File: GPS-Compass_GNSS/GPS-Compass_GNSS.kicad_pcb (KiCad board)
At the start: 4 copper layers, 100 x 146.2 mm, 108 parts, among them IC1 TPS565242DRLR, J2 SMA_F, J2 USB_TypeC, J3 Conn_01x10_Socket, Q3 Q_NMOS_GSD, Q4 BC337, SW1 GNSS_RST, U1 ESP32-S3-WROOM-1, U10 BGA725L6E6327FTSA1, U11 TESEO-LIV3R, U2 AP62300Z6, U3 BQ25887, U4 DRV8834RGER, U9 USBLC6-2SC6

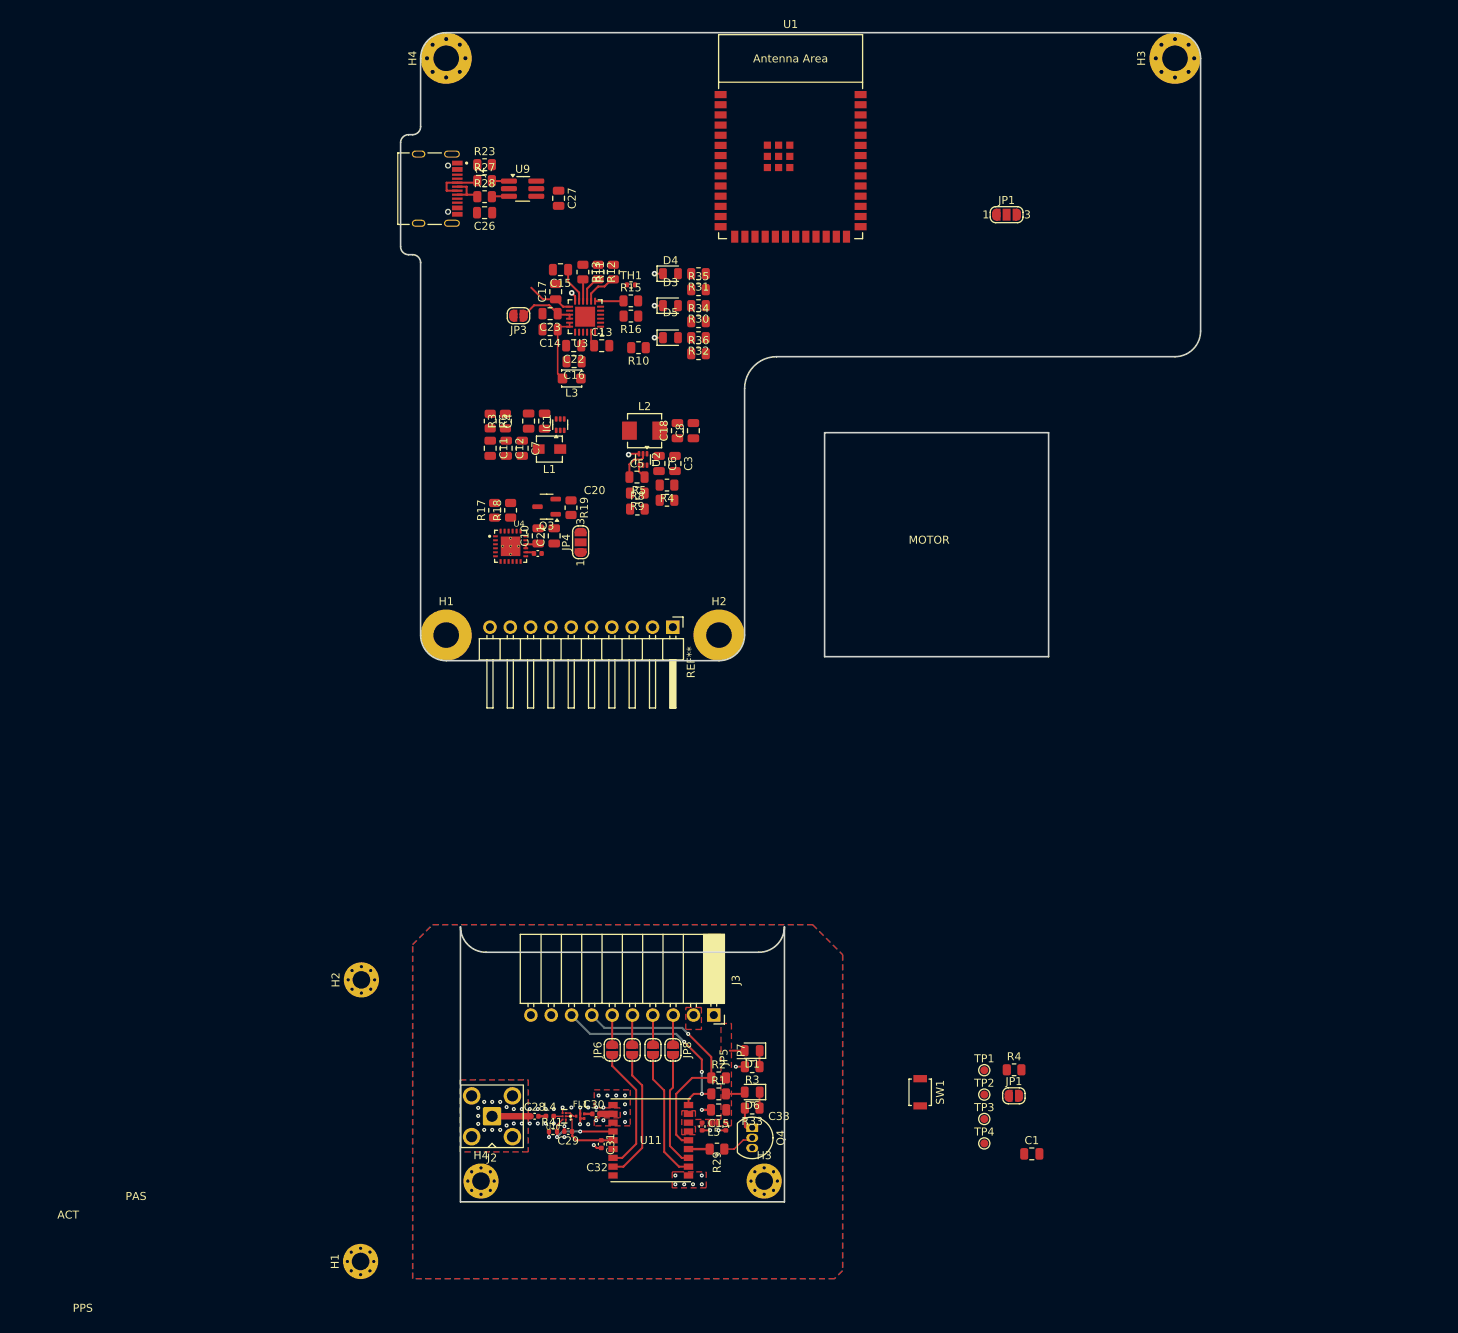
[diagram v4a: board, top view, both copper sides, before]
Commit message: soldermask via fencing
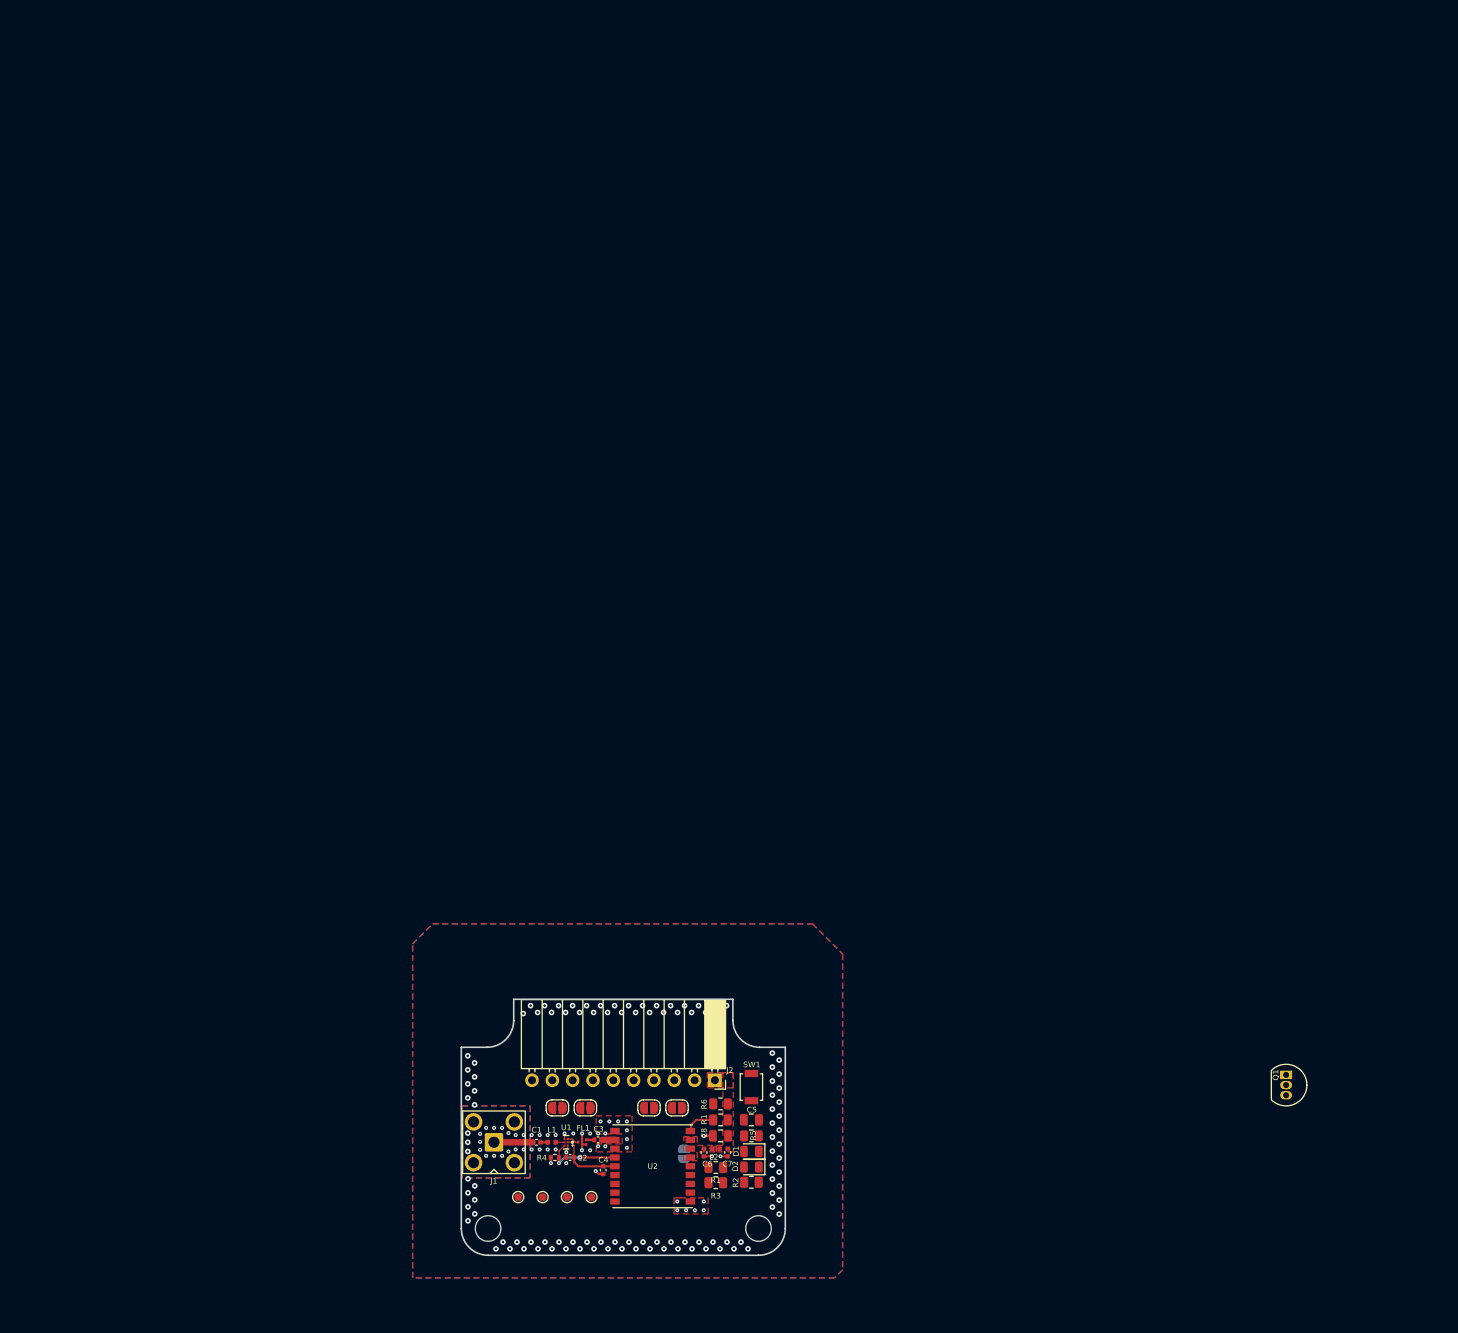
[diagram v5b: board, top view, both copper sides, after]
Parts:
- removed the C1 at (169.9, 110.5)
- removed C10, C16, C17: 10uF, Capacitor_SMD:C_0805_2012Metric
- removed C11, C12, C18: 22uF, Capacitor_SMD:C_0805_2012Metric
- removed C13: 1uF, Capacitor_SMD:C_0805_2012Metric
- removed C14: 47nF, Capacitor_SMD:C_0805_2012Metric
- removed C15: 4.7uF, Capacitor_SMD:C_0805_2012Metric
- removed C20: 10nF, Capacitor_SMD:C_0402_1005Metric
- removed C21, C22, C26, C27, C9: 100nF, Capacitor_SMD:C_0805_2012Metric
- removed C23: 44uF, Capacitor_SMD:C_0805_2012Metric
- removed the C3 at (125.3, 24.2)
- removed the C4 at (107.0, 18.9)
- removed the C6 at (123.3, 24.2)
- removed the C7 at (106.2, 22.3)
- removed the C8 at (127.7, 20.1)
- removed D3, D4, D5: LED, LED_SMD:LED_0805_2012Metric
- removed H1, H3: MountingHole_Pad, MountingHole:MountingHole_2.2mm_M2_Pad_Via
- removed H1: Mounting Hole M3, MountingHole:MountingHole_3.2mm_M3_Pad
- removed the H2 at (130.8, 45.6)
- removed the H2 at (86.2, 88.8)
- removed H3: Mounting Hole M3, MountingHole:MountingHole_3.2mm_M3_Pad_Via
- removed the H4 at (96.8, -26.4)
- removed the H4 at (101.1, 113.9)
- removed IC1: TPS565242DRLR, Package_TO_SOT_SMD:SOT-563
- removed the J2 at (93.3, -10.2)
- removed the JP1 at (166.8, -6.90)
- removed the JP1 at (167.7, 103.2)
- removed JP6, JP7, JP8: Jumper_2_Small_Open, Jumper:SolderJumper-2_P1.3mm_Open_RoundedPad1.0x1.5mm
- removed the L1 at (109.7, 22.4)
- removed the L2 at (121.5, 20.1)
- removed L3: 1uH, Inductor_SMD:L_Walsin_WLFM201609x
- removed Q3: Q_NMOS_GSD, Package_TO_SOT_SMD:SOT-23-3
- removed R10, R19, R34, R35, R36, R9: 10k, Resistor_SMD:R_0805_2012Metric
- removed R11: 383R, Resistor_SMD:R_0805_2012Metric
- removed R12: 300R, Resistor_SMD:R_0805_2012Metric
- removed R13: 9.5R, Resistor_SMD:R_0805_2012Metric
- removed R15: 5.23k, Resistor_SMD:R_0805_2012Metric
- removed R16: 30.1k, Resistor_SMD:R_0805_2012Metric
- removed R17, R18: R(SET), Resistor_SMD:R_0805_2012Metric
- removed R23: 100k, Resistor_SMD:R_0805_2012Metric
- removed R27, R28: 15R, Resistor_SMD:R_0805_2012Metric
- removed the R3 at (104.2, 18.9)
- removed R30, R31, R32: 2.2k, Resistor_SMD:R_0805_2012Metric
- removed the R4 at (124.3, 26.9)
- removed the R4 at (167.7, 100.0)
- removed the R6 at (102.2, 18.9)
- removed R8: 52.3k, Resistor_SMD:R_0805_2012Metric
- removed REF**: PinHeader_1x10_P2.54mm_Horizontal, Connector_PinHeader_2.54mm:PinHeader_1x10_P2.54mm_Horizontal
- removed TH1: 10k NTC, Resistor_SMD:R_0402_1005Metric
- removed the U1 at (139.8, -13.7)
- removed the U2 at (121.3, 23.7)
- removed U3: BQ25887, Package_DFN_QFN:VQFN-24-1EP_4x4mm_P0.5mm_EP2.5x2.5mm
- removed U4: DRV8834RGER, gps-compass_brd:DRIVER_DRV8834RGER
- removed U9: USBLC6-2SC6, Package_TO_SOT_SMD:TSOT-23-6_HandSoldering
- added H2: MountingHole_Pad, MountingHole:MountingHole_3.2mm_M3, F.Cu at (102.0, 119.8)
- added H4: MountingHole_Pad, MountingHole:MountingHole_3.2mm_M3, F.Cu at (135.8, 119.8)
- added JP1: Jumper_2_Small_Open, Jumper:SolderJumper-2_P1.3mm_Open_RoundedPad1.0x1.5mm, F.Cu at (114.2, 104.8)
- added JP2: Jumper_2_Small_Open, Jumper:SolderJumper-2_P1.3mm_Open_RoundedPad1.0x1.5mm, F.Cu at (110.7, 104.8)
- C5: value 100nF -> 100n
- JP3: value Jumper -> Jumper_2_Small_Open; moved to B.Cu
- JP4: value Jumper -> Jumper_2_Small_Open; footprint Jumper:SolderJumper-3_P1.3mm_Open_RoundedPad1.0x1.5mm_NumberLabels -> Jumper:SolderJumper-2_P1.3mm_Open_RoundedPad1.0x1.5mm
- R5: value 52.3k -> 10k
- moved JP3 106.8 mm to (126.5, 110.5), turned to -90 degrees
- moved C5 81.6 mm to (134.9, 106.2)
- moved R5 80.1 mm to (134.9, 108.2), turned to 180 degrees
- moved JP4 71.2 mm to (122.1, 104.8), turned to 180 degrees
- moved Q1 67.1 mm to (201.7, 100.6)
- moved TP2 59.7 mm to (105.8, 115.9), turned to 90 degrees
- moved TP3 56.1 mm to (108.8, 115.9), turned to 90 degrees
- moved TP4 52.6 mm to (111.8, 115.9), turned to 90 degrees
- moved TP1 51.6 mm to (114.9, 115.9), turned to 90 degrees
- moved SW1 21.1 mm to (134.9, 102.2)
- moved R3 15.2 mm to (130.4, 114.1)
- moved D2 14.6 mm to (134.9, 112.2)
- moved R2 9.28 mm to (134.9, 114.0)
- moved JP5 9.16 mm to (125.6, 104.8), turned to 180 degrees
- moved J2 8.15 mm to (130.3, 101.3)
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- renumbered C28 to C1, C29 to C2, C30 to C3, C31 to C4, C32 to C6, C33 to C7, C15 to C8, D6 to D1, D1 to D2, J2 to J1, J3 to J2, L4 to L1, L5 to L2, Q4 to Q1, R29 to R1, R33 to R2, R41 to R4, R2 to R6, U10 to U1, U11 to U2
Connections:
- C5 pad 1: /POWER/SW -> GNSS_RST
- C5 pad 2: Net-(U2-BST) -> GND
- C6 pad 1: Net-(JP1-A) -> Net-(JP3-A)
- J2 pad 1: GND -> +3V3
- J2 pad 2: +3V3 -> GND
- JP3 pad 1: SNS -> Net-(JP3-A)
- JP3 pad 2: SNS_MCU -> Net-(JP3-B)
- JP4 pad 1: +3V3 -> GNSS_TX
- JP4 pad 2: VM -> Net-(JP4-B)
- JP5 pad 1: Net-(JP5-A) -> GNSS_RX
- JP5 pad 2: SCL -> Net-(JP5-B)
- L2 pad 2: Net-(JP1-A) -> Net-(JP3-A)
- R5 pad 1: Net-(U2-EN) -> GNSS_RST
- R5 pad 2: GND -> +3V3
- TP1 pad 1: GNSS_WKP -> VCC_RF
- TP2 pad 1: ANT_OFF -> GNSS_WKP
- TP3 pad 1: GNSS_PPS -> ANT_OFF
- TP4 pad 1: VCC_RF -> GNSS_PPS
- U2 pad 17: Net-(JP5-A) -> Net-(JP1-A)
- U2 pad 2: Net-(JP7-B) -> Net-(JP4-B)
- U2 pad 3: Net-(JP8-B) -> Net-(JP5-B)
- U2 pad 6: Net-(JP1-B) -> Net-(JP3-B)
- U2 pad 7: Net-(JP1-A) -> Net-(JP3-A)
- U2 pad 8: Net-(JP1-A) -> Net-(JP3-A)
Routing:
- net GNSS_WKP: track 31.8 -> 0.00 mm, vias 1 -> 0
- net GNSS_RST: track 26.7 -> 3.83 mm, vias 3 -> 0
- net Net-(JP5-A): track 16.7 -> 0.00 mm
- net Net-(JP7-B): track 16.5 -> 0.00 mm
- net Net-(JP2-A): track 16.0 -> 0.00 mm
- net Net-(JP8-B): track 14.5 -> 0.00 mm
- net SWC: track 8.49 -> 0.00 mm
- net SNS: track 7.26 -> 0.00 mm
- net D- IN: track 6.28 -> 0.00 mm
- net VBATT: track 5.77 -> 0.00 mm
- net D+ IN: track 4.76 -> 0.00 mm
- net LDO: track 4.51 -> 0.00 mm
- net Net-(U3-ILIM): track 4.47 -> 0.00 mm
- net GNSS_TX: track 4.18 -> 0.00 mm
- net /POWER/SW: track 4.14 -> 0.00 mm
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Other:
- board size 100 x 146.2 mm -> 40.5 x 32 mm
- board text removed: "ACT"
- board text removed: "MOTOR"
- board text removed: "PAS"
- board text removed: "PPS"

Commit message: finished
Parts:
- removed JP3: Jumper_2_Small_Open, Jumper:SolderJumper-2_P1.3mm_Open_RoundedPad1.0x1.5mm
- removed the R1 at (131.0, 106.2)
- added G***: LOGO, sumec_graphic:TITANFALL_ART, F.Cu at (108.5, 121.7)
- added G***: LOGO, sumec_graphic:APERTURE_ART, B.Cu at (119.2, 108.0)
- Q1: value BC337 -> MMBT3904; footprint Package_TO_SOT_THT:TO-92_Inline -> Package_TO_SOT_SMD:SOT-23
- moved Q1 73.0 mm to (130.7, 117.2)
- moved TP2 23.8 mm to (126.8, 104.8), turned to -90 degrees
- moved TP4 17.2 mm to (128.6, 119.6), turned to -90 degrees
- moved R6 8.04 mm to (130.2, 112.2)
- moved JP2 5.60 mm to (116.2, 104.8), turned to 90 degrees
- moved R3 5.52 mm to (134.4, 110.2)
- moved R5 5.04 mm to (130.2, 106.3), turned to 0 degrees
- moved JP1 4.60 mm to (118.8, 104.8), turned to 90 degrees
- moved D2 3.93 mm to (134.4, 108.2)
- moved TP3 3.35 mm to (110.8, 113.2), turned to -90 degrees
- moved TP1 2.80 mm to (114.0, 113.2), turned to -90 degrees
- moved D1 2.11 mm to (134.4, 112.2)
- moved R1 2.06 mm to (130.2, 114.2)
- moved JP5 1.10 mm to (124.5, 104.8), turned to -90 degrees
- moved C5 0.90 mm to (134.4, 105.5)
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- renumbered H2 to H1, H4 to H2
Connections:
- C6 pad 1: Net-(JP3-A) -> Net-(U2-VBATT)
- J2 pad 3: GNSS_RX -> GNSS_RST
- J2 pad 4: GNSS_TX -> GNSS_WKP
- J2 pad 5: SCL -> GNSS_RX
- J2 pad 6: SDA -> GNSS_TX
- J2 pad 7: GNSS_WKP -> SCL
- J2 pad 8: GNSS_RST -> SDA
- J2 pad 9: unconnected-(J2-Pin_9-Pad9) -> GND
- L2 pad 2: Net-(JP3-A) -> Net-(U2-VBATT)
- Q1 pad 1: Net-(Q1-C) -> Net-(Q1-B)
- Q1 pad 2: Net-(Q1-B) -> GND
- Q1 pad 3: GND -> Net-(Q1-C)
- U2 pad 6: Net-(JP3-B) -> Net-(U2-VBATT)
- U2 pad 7: Net-(JP3-A) -> Net-(U2-VBATT)
- U2 pad 8: Net-(JP3-A) -> Net-(U2-VBATT)
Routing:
- net GNSS_WKP: track 0.00 -> 16.7 mm
- net Net-(JP2-A): track 0.00 -> 14.2 mm, vias 0 -> 2
- net Net-(JP1-A): track 0.00 -> 13.9 mm
- net GNSS_RST: track 3.83 -> 17.7 mm, vias 0 -> 2
- net Net-(JP4-B): track 0.00 -> 12.8 mm
- net Net-(JP5-B): track 0.00 -> 10.8 mm
- net +3V3: track 0.14 -> 10.3 mm, vias 0 -> 2
- net GNSS_PPS: track 0.00 -> 9.84 mm, vias 0 -> 2
- net Net-(Q1-C): track 0.00 -> 5.65 mm
- net GNSS_RX: track 0.00 -> 5.55 mm
- net GNSS_TX: track 0.00 -> 5.52 mm
- net SDA: track 0.00 -> 4.94 mm
- net SCL: track 0.00 -> 4.81 mm
- net Net-(Q1-B): track 0.00 -> 2.09 mm
- net Net-(D2-K): track 0.00 -> 2.01 mm
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- added copper zone on F.Cu, net Net-(U2-VBATT)
- removed copper zone on F.Cu, net Net-(JP1-A)
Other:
- copper layers 4 -> 2
- board text added: "ANT_O"
- board text added: "PASSIVE"
- board text added: "PPS"
- board text added: "RST"
- board text added: "RX"
- board text added: "SCL"
- board text added: "SDA"
- board text added: "SMA-F"
- board text added: "TESEO-LIV3R GNSS MODULE"
- board text added: "TX"
- board text added: "VCC"
- board text added: "VCC_RF"
- board text added: "WKP"
- board text added: "made by bismarx"

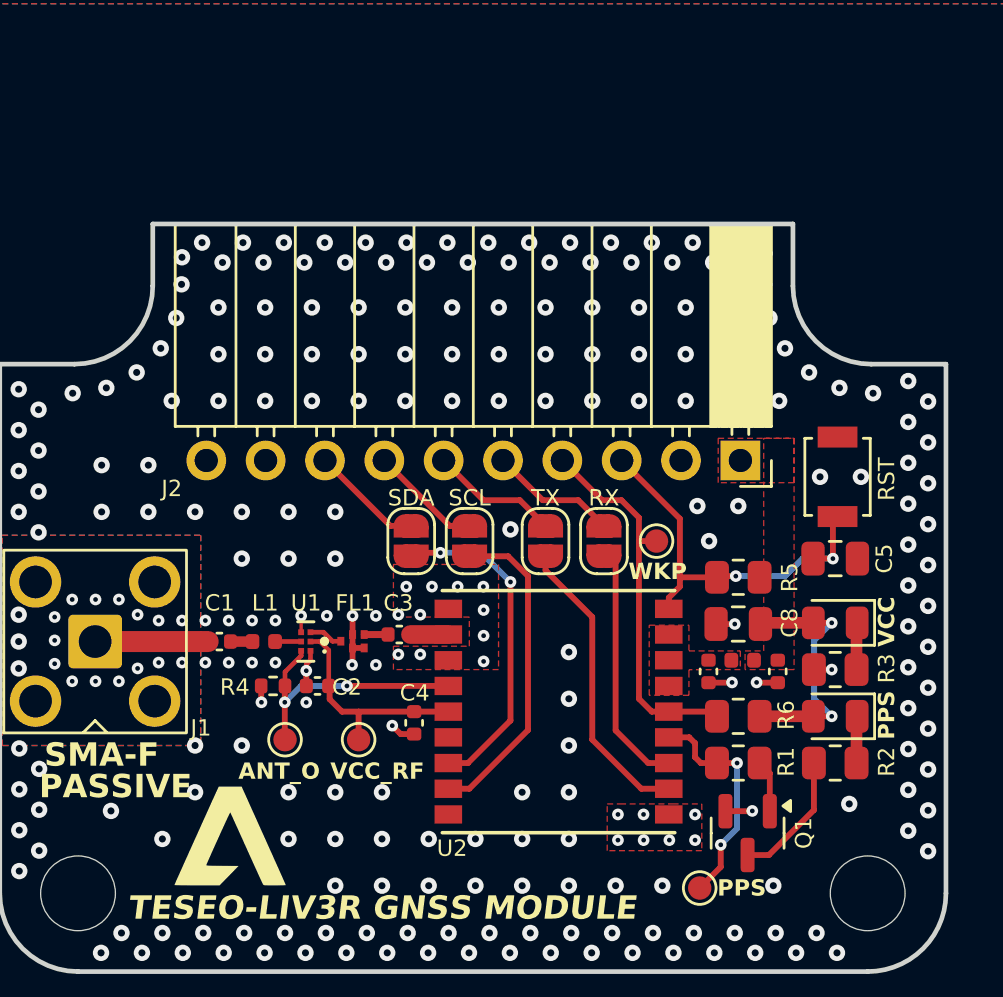
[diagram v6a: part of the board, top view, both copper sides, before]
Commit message: changed socket to header for breadboard pluggablity
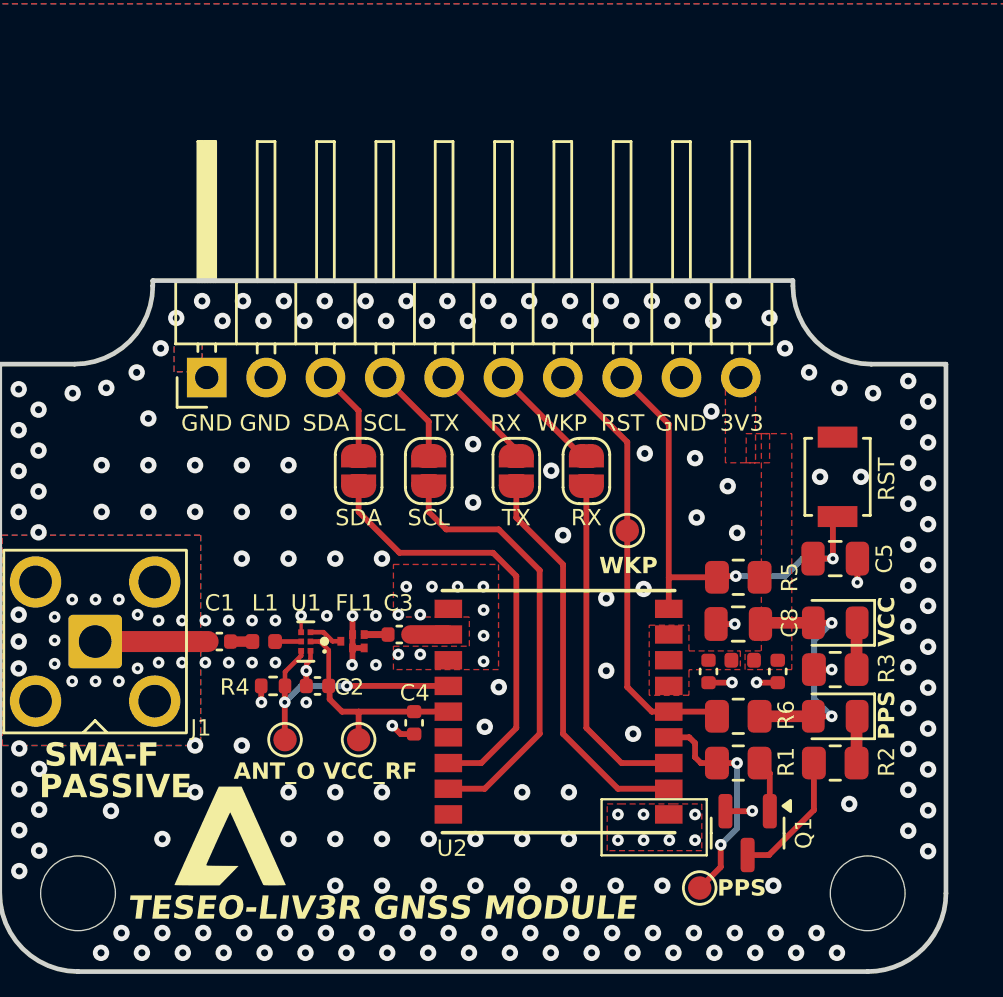
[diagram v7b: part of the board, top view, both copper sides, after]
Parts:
- removed J2: Conn_01x10_Socket, Connector_PinSocket_2.54mm:PinSocket_1x10_P2.54mm_Horizontal
- added J3: 01x10, Connector_PinHeader_2.54mm:PinHeader_1x10_P2.54mm_Horizontal, F.Cu at (107.5, 97.8)
- moved JP2 3.75 mm to (114.0, 101.8)
- moved JP1 3.47 mm to (117.0, 101.8)
- moved JP4 3.25 mm to (120.8, 101.8)
- moved JP5 3.09 mm to (123.8, 101.8)
- moved TP2 1.33 mm to (125.5, 104.3)
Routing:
- net Net-(JP1-A): track 13.9 -> 18.8 mm
- net Net-(JP2-A): track 14.2 -> 19.0 mm, vias 2 -> 0
- net Net-(JP4-B): track 12.8 -> 16.9 mm
- net Net-(JP5-B): track 10.8 -> 14.5 mm
- net GNSS_RST: track 17.7 -> 21.3 mm
- net GNSS_WKP: track 16.7 -> 18.7 mm
- net GND: track 11.1 -> 12.1 mm, vias 261 -> 233
- net SDA: track 4.94 -> 3.94 mm
- net GNSS_TX: track 5.52 -> 4.63 mm
- net SCL: track 4.81 -> 4.13 mm
- net GNSS_RX: track 5.55 -> 4.94 mm
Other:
- board size 40.5 x 32 mm -> 40.5 x 29.6 mm
- board text added: "3V3"
- board text added: "GND"

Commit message: schematric remake
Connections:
- net ANT_OFF renamed /ANT_OFF
- net GNSS_ANT renamed /GNSS_ANT
- net GNSS_PPS renamed /GNSS_PPS
- net GNSS_RST renamed /GNSS_RST
- net GNSS_RX renamed /GNSS_RX
- net GNSS_TX renamed /GNSS_TX
- net GNSS_WKP renamed /GNSS_WKP
- net RF_IN renamed /RF_IN
- net SCL renamed /SCL
- net SDA renamed /SDA
- net VCC_RF renamed /VCC_RF
